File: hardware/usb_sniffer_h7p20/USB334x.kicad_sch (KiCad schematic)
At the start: 24 parts, among them J2 USB_C_Receptacle_USB2.0_16P, J3 USB_A, U2 LM2903, U3 LM2903, U4 LM2903, U5 USB3343, Y1 26M,NC

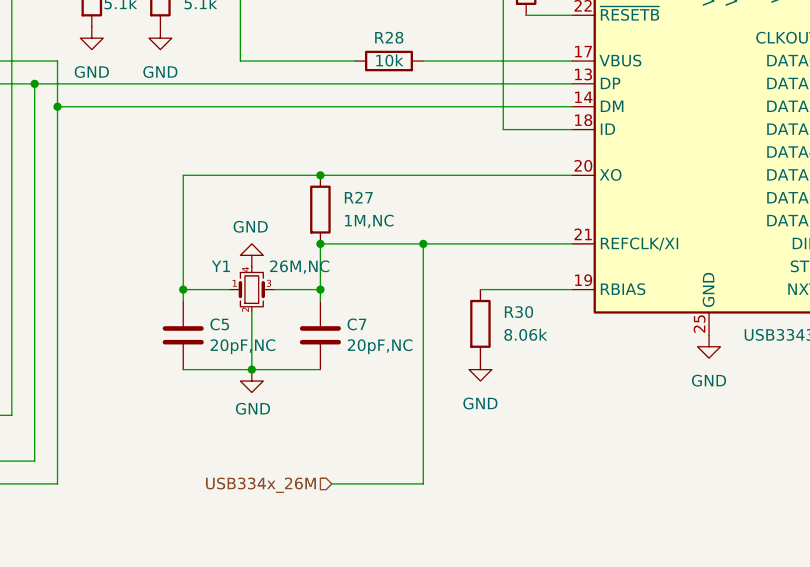
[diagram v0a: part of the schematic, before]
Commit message: 增加辅助电路和优化焊盘工艺
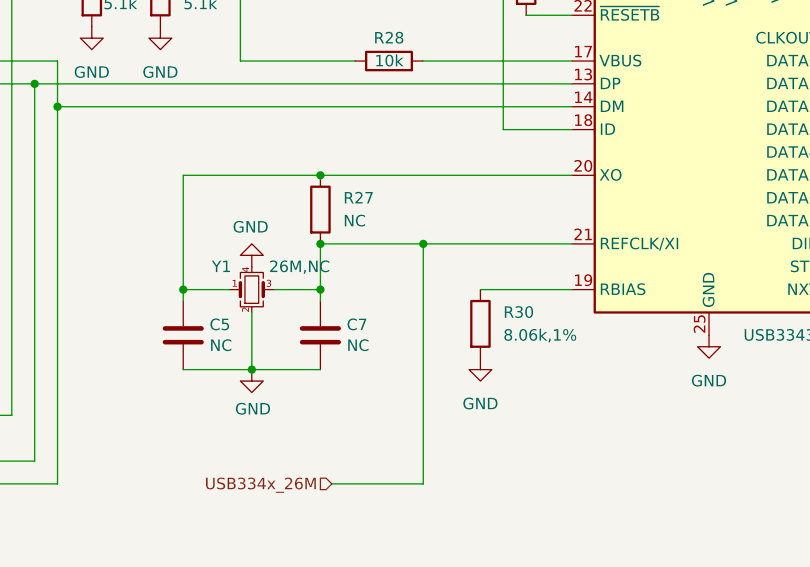
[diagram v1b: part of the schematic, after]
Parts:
- C5, C7: value 20pF,NC -> NC; footprint vllogic:C_0402_6mil -> Capacitor_SMD:C_0402_1005Metric
- R27: value 1M,NC -> NC
- R30: value 8.06k -> 8.06k,1%
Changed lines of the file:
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@@
       (effects (font (size 1.27 1.27)) (justify left))
     )
-    (property "Value" "8.06k" (at 175.26 99.06 0)
+    (property "Value" "8.06k,1%" (at 175.26 99.06 0)
       (effects (font (size 1.27 1.27)) (justify left))
     )
@@
       (effects (font (size 1.27 1.27)) (justify left))
     )
-    (property "Value" "1M,NC" (at 157.48 86.36 0)
+    (property "Value" "NC" (at 157.48 86.36 0)
       (effects (font (size 1.27 1.27)) (justify left))
     )
@@
       (effects (font (size 1.27 1.27)) (justify right))
     )
-    (property "Value" "20pF,NC" (at 142.621 100.203 0)
-      (effects (font (size 1.27 1.27)) (justify right))
-    )
-    (property "Footprint" "vllogic:C_0402_6mil" (at 138.7348 95.25 0)
+    (property "Value" "NC" (at 142.621 100.203 0)
+      (effects (font (size 1.27 1.27)) (justify right))
+    )
+    (property "Footprint" "Capacitor_SMD:C_0402_1005Metric" (at 138.7348 95.25 0)
       (effects (font (size 1.27 1.27)) hide)
     )
@@
       (effects (font (size 1.27 1.27)) (justify right))
     )
-    (property "Value" "20pF,NC" (at 157.861 100.203 0)
-      (effects (font (size 1.27 1.27)) (justify right))
-    )
-    (property "Footprint" "vllogic:C_0402_6mil" (at 153.9748 95.25 0)
-      (effects (font (size 1.27 1.27)) hide)
-    )
+    (property "Value" "NC" (at 157.861 100.203 0)
+      (effects (font (size 1.27 1.27)) (justify right))
+    )
+    (property "Footprint" "Capacitor_SMD:C_0402_1005Metric" (at 153.9748 95.25 0)
+      (effects (font (size 1.27 1.27)) hide)
+    )

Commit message: hardware\usb_sniffer_h7p20\production_files.2025605
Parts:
- R20, R28, R31: value 10k -> 10k,1%
- R21: value 33k -> 33k,1%
- R25, R26: value 5.1k -> 5.1k,1%
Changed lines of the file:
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@@
       (effects (font (size 1.27 1.27)) (justify left))
     )
-    (property "Value" "10k" (at 180.34 60.96 0)
+    (property "Value" "10k,1%" (at 180.34 60.96 0)
       (effects (font (size 1.27 1.27)) (justify left))
     )
@@
       (effects (font (size 1.27 1.27)))
     )
-    (property "Value" "10k" (at 162.56 68.58 90)
+    (property "Value" "10k,1%" (at 162.56 68.58 90)
       (effects (font (size 1.27 1.27)))
     )
@@
       (effects (font (size 1.27 1.27)) (justify left))
     )
-    (property "Value" "33k" (at 26.67 102.87 0)
+    (property "Value" "33k,1%" (at 26.67 102.87 0)
       (effects (font (size 1.27 1.27)) (justify left))
     )
@@
       (effects (font (size 1.27 1.27)) (justify left))
     )
-    (property "Value" "5.1k" (at 139.7 62.23 0)
+    (property "Value" "5.1k,1%" (at 139.7 62.23 0)
       (effects (font (size 1.27 1.27)) (justify left))
     )
@@
       (effects (font (size 1.27 1.27)) (justify left))
     )
-    (property "Value" "5.1k" (at 130.81 62.23 0)
+    (property "Value" "5.1k,1%" (at 130.81 62.23 0)
       (effects (font (size 1.27 1.27)) (justify left))
     )
@@
       (effects (font (size 1.27 1.27)) (justify left))
     )
-    (property "Value" "10k" (at 26.67 92.71 0)
-      (effects (font (size 1.27 1.27)) (justify left))
-    )
+    (property "Value" "10k,1%" (at 26.67 92.71 0)
+      (effects (font (size 1.27 1.27)) (justify left))
+    )

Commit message: [usb_sniffer_h7p20] 结构优化与验证
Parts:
- J3: footprint vllogic:USB-AF-180 -> vllogic:USB-AF_YIJIAN
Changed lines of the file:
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@@
       (effects (font (size 1.27 1.27)))
     )
-    (property "Footprint" "vllogic:USB-AF-180" (at 105.41 114.3 0)
+    (property "Footprint" "vllogic:USB-AF_YIJIAN" (at 105.41 114.3 0)
       (effects (font (size 1.27 1.27)) hide)
     )

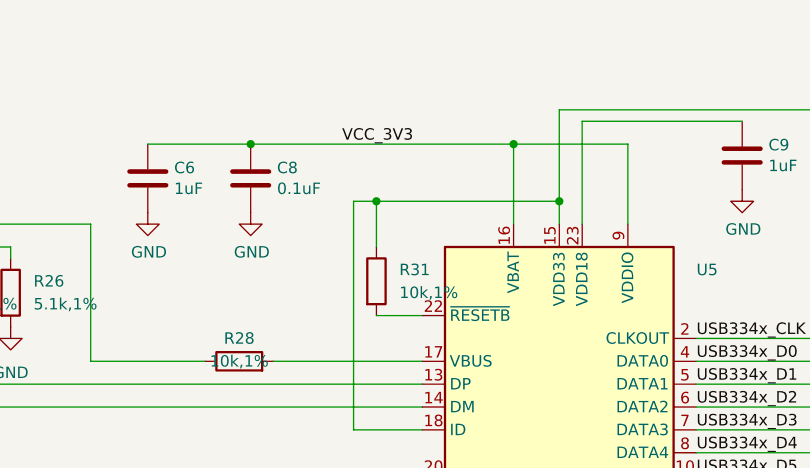
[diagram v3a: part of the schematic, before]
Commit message: [usb_sniffer_h7p20] 修复USB3343参考时钟电路错误；修复USB3343 RESET脚上拉错误
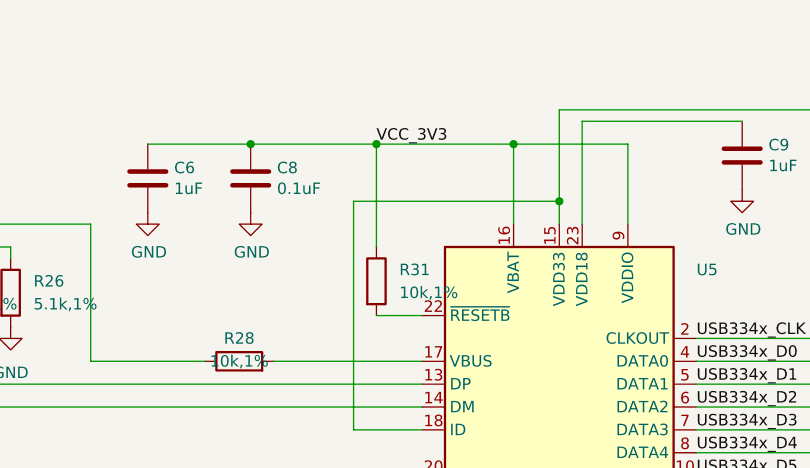
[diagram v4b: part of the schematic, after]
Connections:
- net VCC_3V3: now also R31.1
- net at C10.2, U5.15 (VDD33), U5.18 (ID): no longer R31.1
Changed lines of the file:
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@@
   (junction (at 125.73 73.66) (diameter 0) (color 0 0 0 0)
   )
-  (junction (at 177.8 50.8) (diameter 0) (color 0 0 0 0)
-  )
   (junction (at 123.19 71.12) (diameter 0) (color 0 0 0 0)
   )
@@
   (junction (at 50.8 106.68) (diameter 0) (color 0 0 0 0)
   )
+  (junction (at 177.8 44.45) (diameter 0) (color 0 0 0 0)
+  )
   (junction (at 154.94 88.9) (diameter 0) (color 0 0 0 0)
   )
@@
     (stroke (width 0) (type default))
   )
-  (wire (pts (xy 177.8 50.8) (xy 177.8 55.88))
-    (stroke (width 0) (type default))
-  )
   (wire (pts (xy 93.98 91.44) (xy 101.6 91.44))
     (stroke (width 0) (type default))
@@
     (stroke (width 0) (type default))
   )
+  (wire (pts (xy 177.8 44.45) (xy 193.04 44.45))
+    (stroke (width 0) (type default))
+  )
   (wire (pts (xy 213.36 83.82) (xy 229.87 83.82))
     (stroke (width 0) (type default))
@@
     (stroke (width 0) (type default))
   )
+  (wire (pts (xy 177.8 44.45) (xy 177.8 55.88))
+    (stroke (width 0) (type default))
+  )
   (wire (pts (xy 40.64 119.38) (xy 52.07 119.38))
     (stroke (width 0) (type default))
@@
     (stroke (width 0) (type default))
   )
-  (wire (pts (xy 175.26 50.8) (xy 177.8 50.8))
+  (wire (pts (xy 175.26 50.8) (xy 198.12 50.8))
     (stroke (width 0) (type default))
   )
@@
     (stroke (width 0) (type default))
   )
-  (wire (pts (xy 177.8 50.8) (xy 198.12 50.8))
-    (stroke (width 0) (type default))
-  )
   (wire (pts (xy 50.8 106.68) (xy 50.8 124.46))
     (stroke (width 0) (type default))
@@
     (stroke (width 0) (type default))
   )
-  (wire (pts (xy 163.83 44.45) (xy 193.04 44.45))
+  (wire (pts (xy 163.83 44.45) (xy 177.8 44.45))
     (stroke (width 0) (type default))
   )
@@
     (effects (font (size 1.27 1.27)) (justify left bottom))
   )
-  (label "VCC_3V3" (at 173.99 44.45 0) (fields_autoplaced)
-    (effects (font (size 1.27 1.27)) (justify left bottom))
-  )
+  (label "VCC_3V3" (at 177.8 44.45 0) (fields_autoplaced)
+    (effects (font (size 1.27 1.27)) (justify left bottom))
+  )

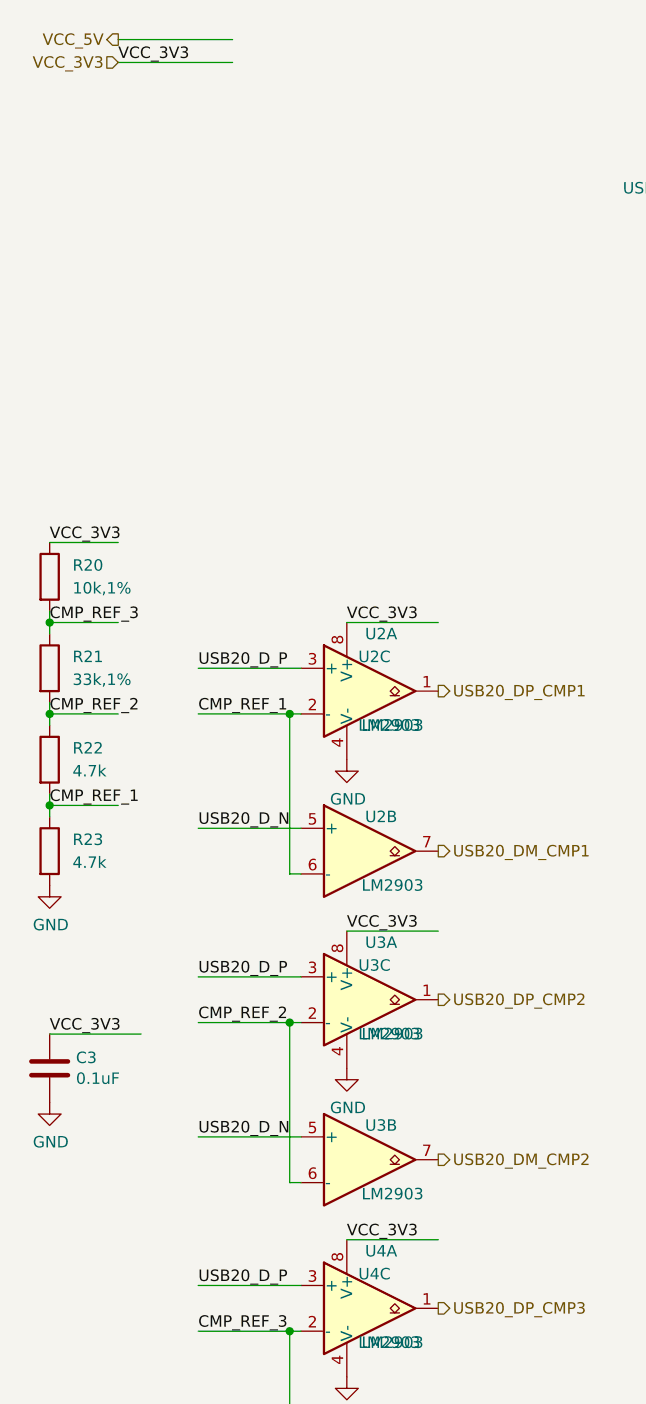
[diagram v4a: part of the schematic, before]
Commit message: [usb_sniffer_h7p20] 使用USB5V驱动LM2903
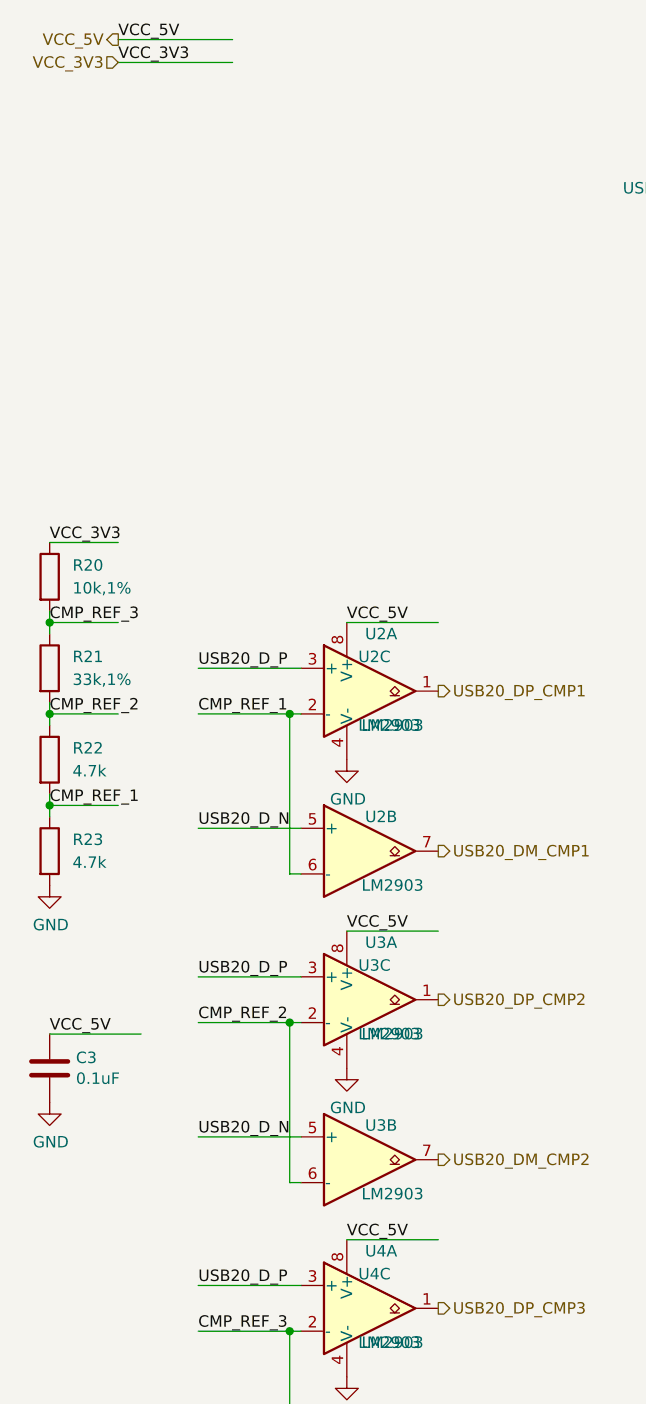
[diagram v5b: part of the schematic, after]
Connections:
- net VCC_3V3: no longer C3.2, U2.8 (V+), U3.8 (V+), U4.8 (V+)
- net VCC_5V: now also C3.2, U2.8 (V+), U3.8 (V+), U4.8 (V+)
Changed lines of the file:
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@@
     (stroke (width 0) (type default))
-  )
-  (label "VCC_3V3" (at 24.13 142.24 0) (fields_autoplaced)
-    (effects (font (size 1.27 1.27)) (justify left bottom))
   )
   (label "USB20_D_N" (at 40.64 153.67 0) (fields_autoplaced)
@@
   )
   (label "USB20_D_N" (at 40.64 119.38 0) (fields_autoplaced)
+    (effects (font (size 1.27 1.27)) (justify left bottom))
+  )
+  (label "VCC_5V" (at 31.75 31.75 0) (fields_autoplaced)
+    (effects (font (size 1.27 1.27)) (justify left bottom))
+  )
+  (label "VCC_5V" (at 57.15 130.81 0) (fields_autoplaced)
     (effects (font (size 1.27 1.27)) (justify left bottom))
   )
@@
     (effects (font (size 1.27 1.27)) (justify left bottom))
   )
+  (label "VCC_5V" (at 57.15 96.52 0) (fields_autoplaced)
+    (effects (font (size 1.27 1.27)) (justify left bottom))
+  )
+  (label "VCC_5V" (at 57.15 165.1 0) (fields_autoplaced)
+    (effects (font (size 1.27 1.27)) (justify left bottom))
+  )
   (label "CMP_REF_3" (at 40.64 175.26 0) (fields_autoplaced)
+    (effects (font (size 1.27 1.27)) (justify left bottom))
+  )
+  (label "VCC_5V" (at 24.13 142.24 0) (fields_autoplaced)
     (effects (font (size 1.27 1.27)) (justify left bottom))
   )
@@
     (effects (font (size 1.27 1.27)) (justify left bottom))
   )
-  (label "VCC_3V3" (at 57.15 165.1 0) (fields_autoplaced)
-    (effects (font (size 1.27 1.27)) (justify left bottom))
-  )
-  (label "VCC_3V3" (at 57.15 96.52 0) (fields_autoplaced)
-    (effects (font (size 1.27 1.27)) (justify left bottom))
-  )
   (label "VCC_3V3" (at 31.75 34.29 0) (fields_autoplaced)
     (effects (font (size 1.27 1.27)) (justify left bottom))
   )
-  (label "VCC_3V3" (at 57.15 130.81 0) (fields_autoplaced)
-    (effects (font (size 1.27 1.27)) (justify left bottom))
-  )

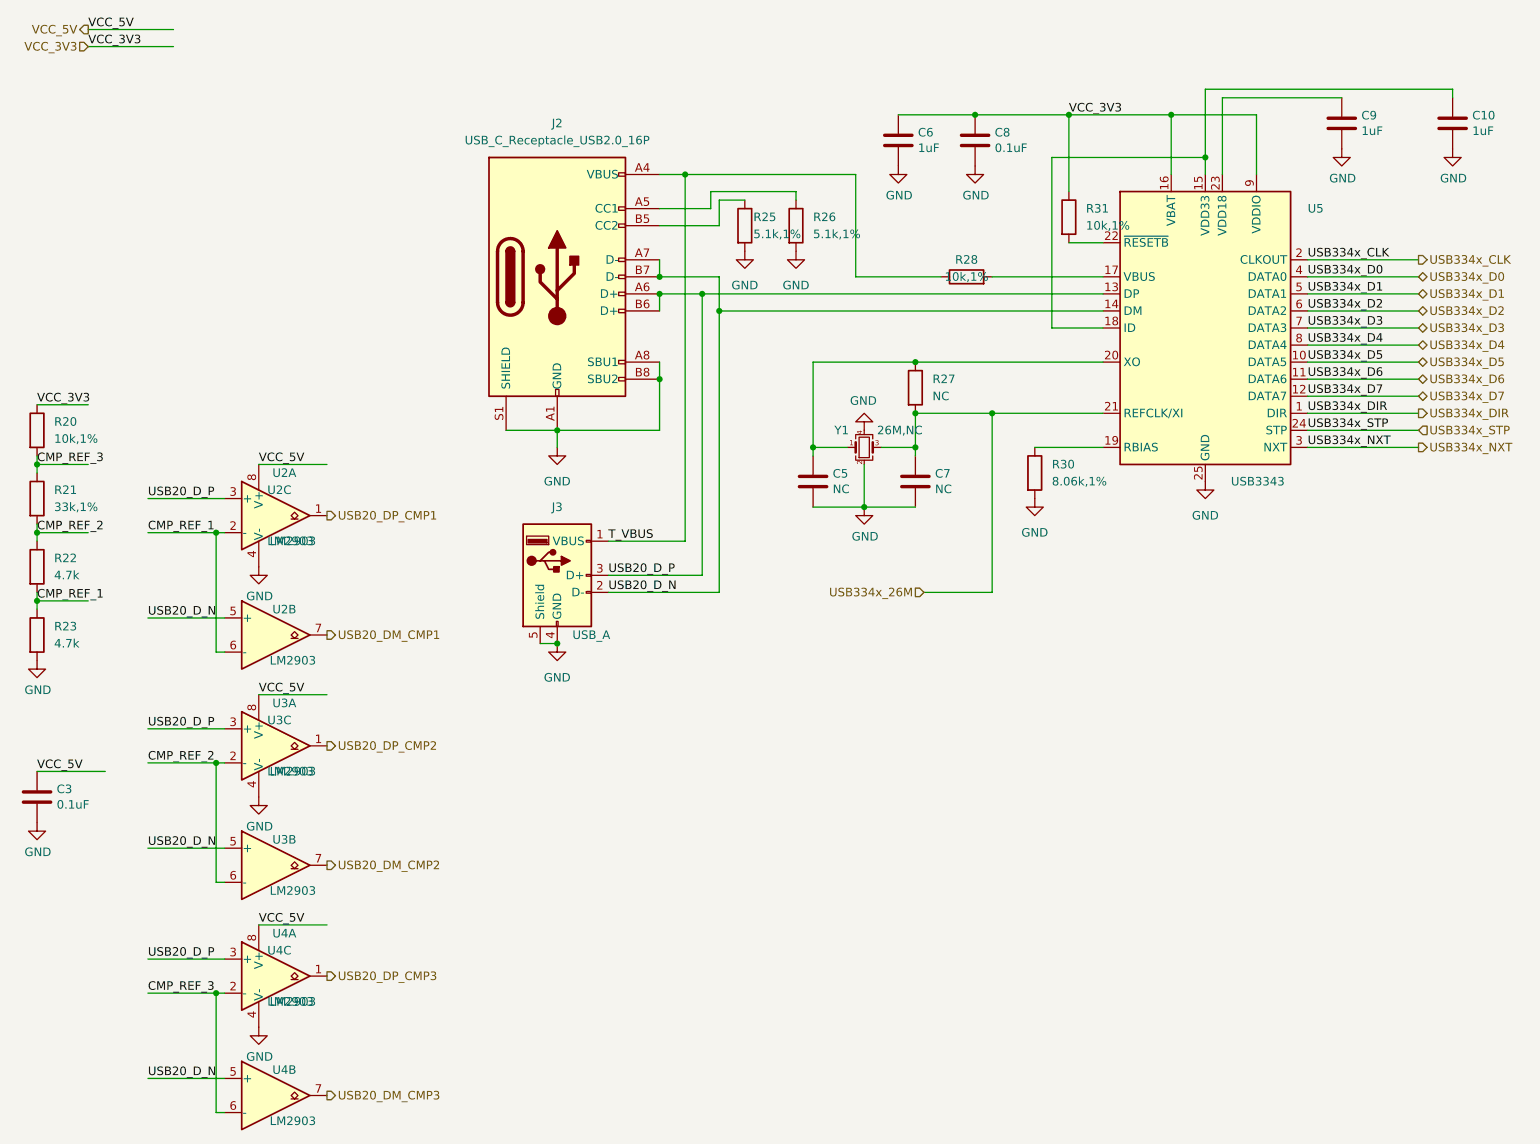
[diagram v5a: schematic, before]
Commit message: [usb_sniffer_h7p20] 移除NC器件，更换LM2903A-VR，双螺丝孔固定
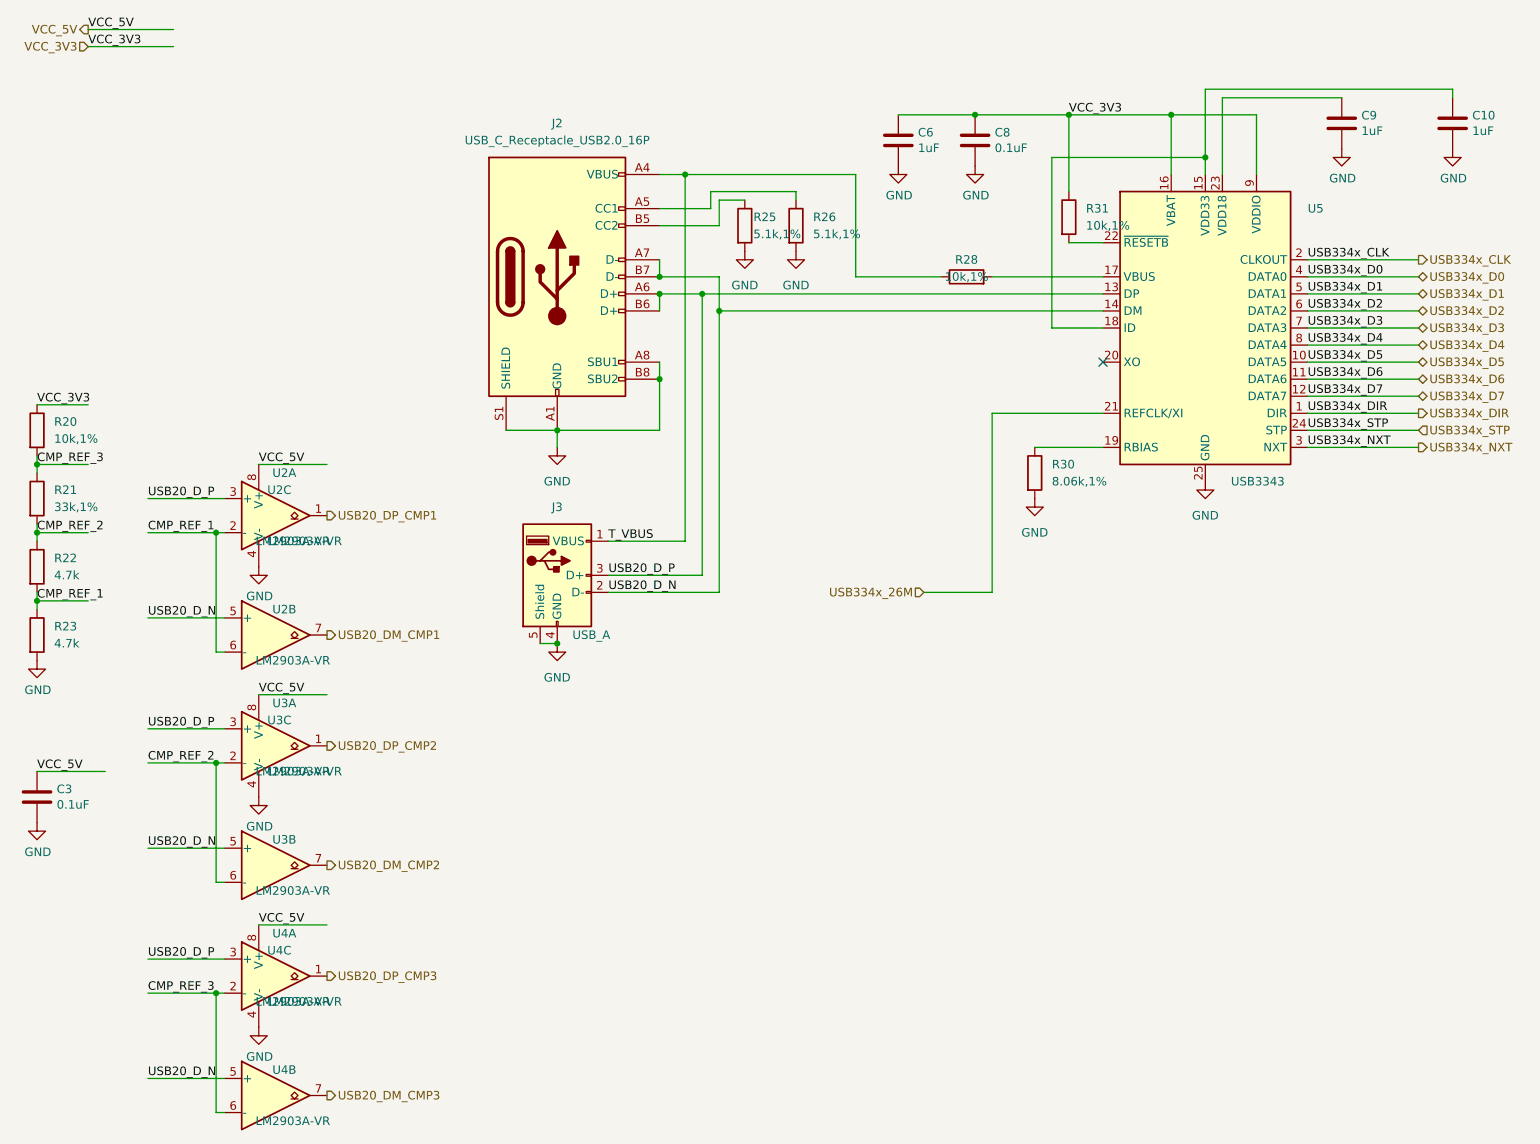
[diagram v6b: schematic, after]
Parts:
- removed C5, C7: NC, Capacitor_SMD:C_0402_1005Metric, symbol Device:C
- removed R27: NC, Resistor_SMD:R_0402_1005Metric, symbol Device:R
- removed Y1: 26M,NC, vllogic:OSC_3225, symbol Device:Crystal_GND24_Small
- U2, U3, U4: value LM2903 -> LM2903A-VR
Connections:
- no-connect marks 0 -> 1
